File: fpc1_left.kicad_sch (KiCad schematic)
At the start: 1 part

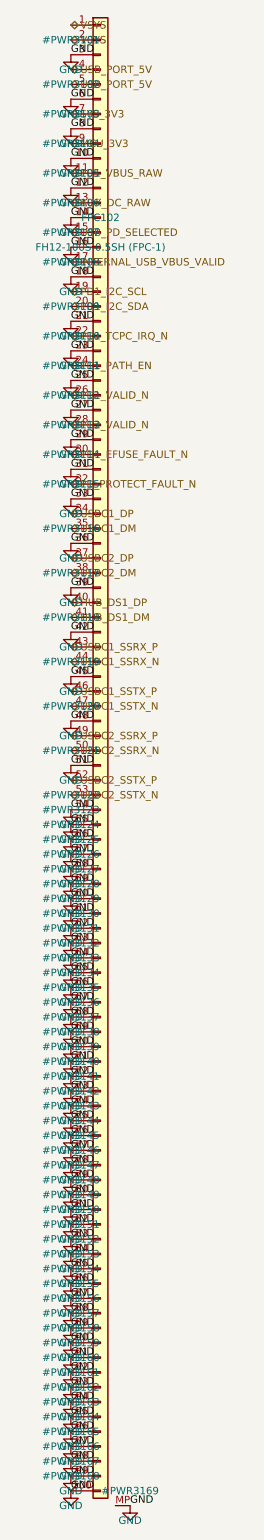
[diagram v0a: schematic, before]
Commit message: Phase 4 deep audit: FH41-68S connectors, placement hygiene, one-shot fixes
Found and fixed four board-killers in the pre-fab audit:

1. Fictional connector: the Hirose FH12 series stops at 60 positions, so
   the 100-pin FH12-100S used for FPC-1/FPC-2 does not exist.  Replaced
   with the FH41-68S-0.5SH(05) (shielded-FFC, 68 positions; FPC-1 uses
   pins 1-53, FPC-2 pins 1-61):
   - new footprint derived from KiCad's FH41-30S (68 signal pads, MP at
     +/-18, 14 SH solder-holds, 38mm body) with SH pads tied to GND
   - new 68-pin symbol (Conn_01x68_FFC_MP), pin maps trimmed to 68
   - fictional FH12-100S footprint/symbol/script removed
   - cable spec updated (68-pin shielded FFC, one type for both)

2. Connector courtyard conflicts: parts sat under connector bodies
   (pads cleared, bodies collided).  Placement now enforces courtyard
   clearance against the connector body; the resolver scans with
   courtyard checks; a double-shift bug that hid re-placed parts' true
   positions was fixed.

3. FPC-3 orientation: the FH12's FPC enters from the +y side; both FPC-3
   connectors faced away from the seam.  FPC105 -> (123.5, 6.5) rot 180,
   FPC106 -> (30, 54) rot 0 so the cable exits the center bottom edge
   and enters the BMS top edge.

4. Original-layout defects: 16 genuine pad-pad shorts (inductor pads
   swallowing caps, passives on each other, parts on mounting holes) and
   23 parts inside the hinge cutouts (physically off the board) are all
   moved to legal spots; zones refilled against the final placement.

New post-build hygiene sweep (fix_board_hygiene.py) uses the final board
text as the geometry oracle, converges to a clean state, and reports
residuals instead of dropping them.

Final DRC: 0 shorts / 0 clearance / 0 hole violations on all four boards
(bms fully clean).  Remaining: courtyard touches around the Mu socket and
M.2 slot (design-inherent moat), chassis-edge copper, zone islands, silk
cosmetics, and unrouted nets (Phase 4b).  Gate: SCHEMATIC R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
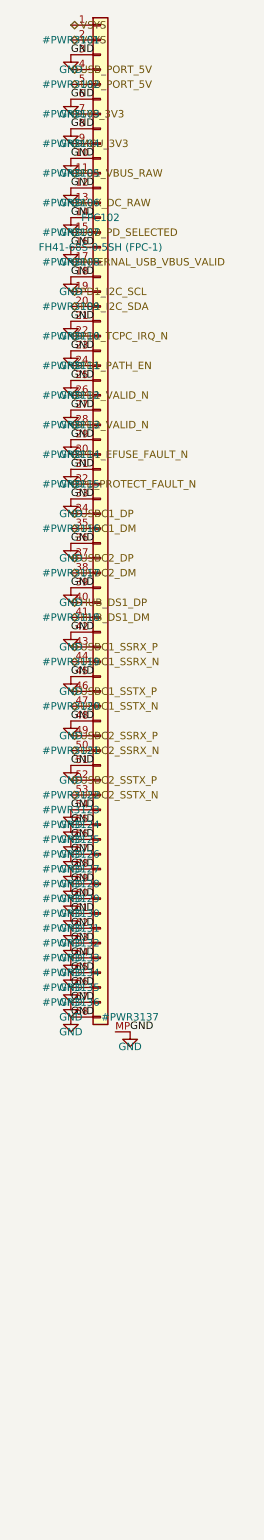
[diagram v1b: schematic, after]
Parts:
- FPC102: value FH12-100S-0.5SH (FPC-1) -> FH41-68S-0.5SH (FPC-1); footprint ducktop2:FH12-100S-0.5SH_1x100-1MP_P0.50mm_Horizontal -> ducktop2:Hirose_FH41-68S-0.5SH_1x68_1MP_1SH_P0.5mm_Horizontal; symbol Conn_01x100_FFC_MP:Conn_01x100_FFC_MP -> Conn_01x68_FFC_MP:Conn_01x68_FFC_MP
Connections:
- net GND: no longer FPC102.100 (Pin_100), FPC102.69 (Pin_69), FPC102.70 (Pin_70), FPC102.71 (Pin_71), FPC102.72 (Pin_72), FPC102.73 (Pin_73), FPC102.74 (Pin_74), FPC102.75 (Pin_75), FPC102.76 (Pin_76), FPC102.77 (Pin_77), FPC102.78 (Pin_78), FPC102.79 (Pin_79), FPC102.80 (Pin_80), FPC102.81 (Pin_81), FPC102.82 (Pin_82), FPC102.83 (Pin_83), FPC102.84 (Pin_84), FPC102.85 (Pin_85), FPC102.86 (Pin_86), FPC102.87 (Pin_87), FPC102.88 (Pin_88), FPC102.89 (Pin_89), FPC102.90 (Pin_90), FPC102.91 (Pin_91), FPC102.92 (Pin_92), FPC102.93 (Pin_93), FPC102.94 (Pin_94), FPC102.95 (Pin_95), FPC102.96 (Pin_96), FPC102.97 (Pin_97), FPC102.98 (Pin_98), FPC102.99 (Pin_99)

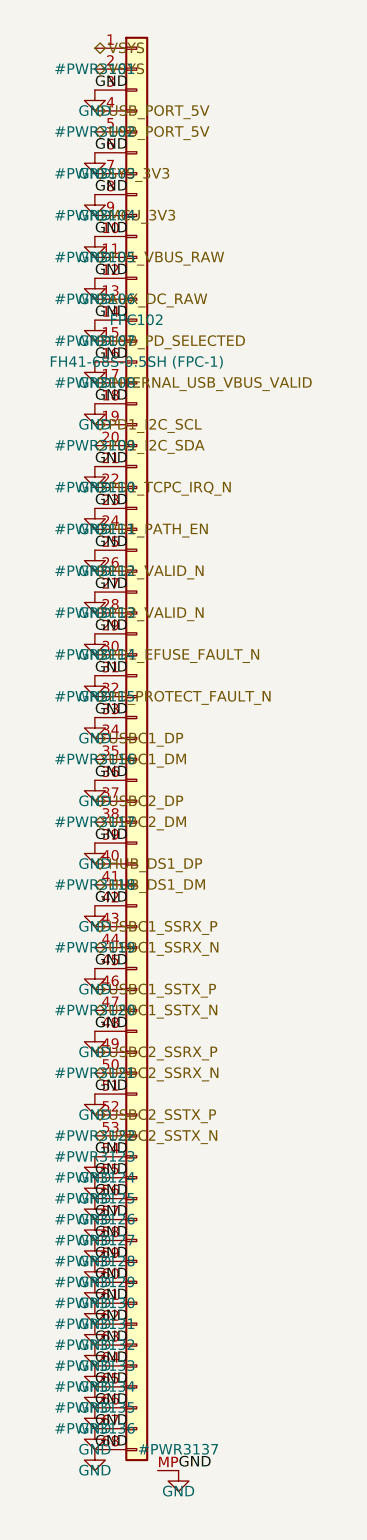
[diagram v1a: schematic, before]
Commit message: Phase 5: second-opinion audit remediation + rebuilt, verified board pipeline
Second-opinion AI audit found A-tier defects; remediation applied and the
board pipeline rebuilt on a known-good base with the fixes it needed:

- electrical: LTC4418IUF symbol pinout corrected (both selectors were
  dead as drawn); center charge cascade (U15 <- U15B, PD1 > PD2 > AUX);
  pack negative never crosses FPC-3, 15-pin FG_VSS return; power-budgeted
  FPC pin maps (0.4 A/pin derate); J12/DS4 completed; AUX source fuse
- FH41-68S footprint: 13 datasheet-correct SH pads + SH pin in symbol
- connector geometry settled against the Hirose FH12 2D drawing: FFC
  enters opposite the solder pins (mouth = local +Y); reversed side-B
  maps are correct for the 180-deg-mounted pairs; rotations set so mouths
  face across every seam
- pipeline (generate_split_boards.py): per-pin pad-net resync from the
  netlists (kills shadow nets for good), netlist-exact name
  normalization, netlist-only part injection (cascade, probe headers),
  zone refill after outline swap, read-before-write race fixed, orphan
  parts dropped loudly, non-zero exit on unresolved overlaps
- monolith board relocated to old/monolith_ducktop2.kicad_pcb (placement
  oracle for the center cut only)

verified end state: 4 boards 0 shorts / 0 clearance / 0 drill, 0 boundary
crossings, 6/6 connectors contract-exact with mouths facing, 0 shadow
nets, gates PASS x4, ERC 0 x4. routing next (499 nets/board).
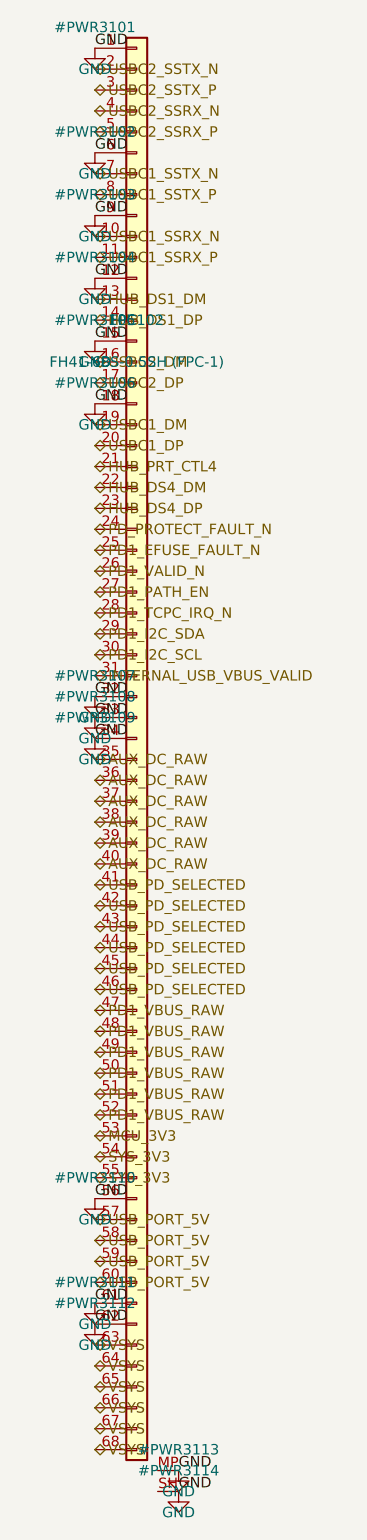
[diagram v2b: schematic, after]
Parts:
- FPC102: MPN (none) -> FH41-68S-0.5SH(05); Manufacturer (none) -> Hirose
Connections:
- net PD2_VALID_N is gone; now on net PD1_TCPC_IRQ_N: FPC102.28 (Pin_28)
- net AUX_DC_RAW: now also FPC102.35 (Pin_35), FPC102.36 (Pin_36), FPC102.37 (Pin_37), FPC102.38 (Pin_38), FPC102.39 (Pin_39), FPC102.40 (Pin_40); no longer FPC102.13 (Pin_13)
- net GND: now also FPC102.1 (Pin_1), FPC102.15 (Pin_15), FPC102.32 (Pin_32), FPC102.34 (Pin_34), FPC102.9 (Pin_9), FPC102.SH; no longer FPC102.10 (Pin_10), FPC102.14 (Pin_14), FPC102.16 (Pin_16), FPC102.21 (Pin_21), FPC102.23 (Pin_23), FPC102.25 (Pin_25), FPC102.27 (Pin_27), FPC102.29 (Pin_29), FPC102.3 (Pin_3), FPC102.31 (Pin_31), FPC102.36 (Pin_36), FPC102.39 (Pin_39), FPC102.42 (Pin_42), FPC102.45 (Pin_45), FPC102.48 (Pin_48), FPC102.51 (Pin_51), FPC102.54 (Pin_54), FPC102.55 (Pin_55), FPC102.57 (Pin_57), FPC102.58 (Pin_58), FPC102.59 (Pin_59), FPC102.60 (Pin_60), FPC102.63 (Pin_63), FPC102.64 (Pin_64), FPC102.65 (Pin_65), FPC102.66 (Pin_66), FPC102.67 (Pin_67), FPC102.68 (Pin_68), FPC102.8 (Pin_8)
- net HUB_DS1_DM: now also FPC102.13 (Pin_13); no longer FPC102.41 (Pin_41)
- net HUB_DS1_DP: now also FPC102.14 (Pin_14); no longer FPC102.40 (Pin_40)
- net INTERNAL_USB_VBUS_VALID: now also FPC102.31 (Pin_31); no longer FPC102.17 (Pin_17)
- net MCU_3V3: now also FPC102.53 (Pin_53); no longer FPC102.9 (Pin_9)
- net PD1_EFUSE_FAULT_N: now also FPC102.25 (Pin_25); no longer FPC102.30 (Pin_30)
- net PD1_I2C_SCL: now also FPC102.30 (Pin_30); no longer FPC102.19 (Pin_19)
- net PD1_I2C_SDA: now also FPC102.29 (Pin_29); no longer FPC102.20 (Pin_20)
- net PD1_PATH_EN: now also FPC102.27 (Pin_27); no longer FPC102.24 (Pin_24)
- net PD1_TCPC_IRQ_N: no longer FPC102.22 (Pin_22)
- net PD1_VBUS_RAW: now also FPC102.47 (Pin_47), FPC102.48 (Pin_48), FPC102.49 (Pin_49), FPC102.50 (Pin_50), FPC102.51 (Pin_51), FPC102.52 (Pin_52); no longer FPC102.11 (Pin_11)
- net PD_PROTECT_FAULT_N: now also FPC102.24 (Pin_24); no longer FPC102.32 (Pin_32)
- net SYS_3V3: now also FPC102.54 (Pin_54), FPC102.55 (Pin_55); no longer FPC102.7 (Pin_7)
- net USBC1_DM: now also FPC102.19 (Pin_19); no longer FPC102.35 (Pin_35)
- net USBC1_DP: now also FPC102.20 (Pin_20); no longer FPC102.34 (Pin_34)
- net USBC1_SSRX_N: now also FPC102.10 (Pin_10); no longer FPC102.44 (Pin_44)
- net USBC1_SSRX_P: now also FPC102.11 (Pin_11); no longer FPC102.43 (Pin_43)
- net USBC1_SSTX_N: now also FPC102.7 (Pin_7); no longer FPC102.47 (Pin_47)
- net USBC1_SSTX_P: now also FPC102.8 (Pin_8); no longer FPC102.46 (Pin_46)
- net USBC2_DM: now also FPC102.16 (Pin_16); no longer FPC102.38 (Pin_38)
- net USBC2_DP: now also FPC102.17 (Pin_17); no longer FPC102.37 (Pin_37)
- net USBC2_SSRX_N: now also FPC102.4 (Pin_4); no longer FPC102.50 (Pin_50)
- net USBC2_SSRX_P: now also FPC102.5 (Pin_5); no longer FPC102.49 (Pin_49)
- net USBC2_SSTX_N: now also FPC102.2 (Pin_2); no longer FPC102.53 (Pin_53)
- net USBC2_SSTX_P: now also FPC102.3 (Pin_3); no longer FPC102.52 (Pin_52)
- net USB_PD_SELECTED: now also FPC102.41 (Pin_41), FPC102.42 (Pin_42), FPC102.43 (Pin_43), FPC102.44 (Pin_44), FPC102.45 (Pin_45), FPC102.46 (Pin_46); no longer FPC102.15 (Pin_15)
- net USB_PORT_5V: now also FPC102.57 (Pin_57), FPC102.58 (Pin_58), FPC102.59 (Pin_59), FPC102.60 (Pin_60); no longer FPC102.4 (Pin_4), FPC102.5 (Pin_5)
- net VSYS: now also FPC102.63 (Pin_63), FPC102.64 (Pin_64), FPC102.65 (Pin_65), FPC102.66 (Pin_66), FPC102.67 (Pin_67), FPC102.68 (Pin_68); no longer FPC102.1 (Pin_1), FPC102.2 (Pin_2)
- new net HUB_DS4_DM: FPC102.22 (Pin_22)
- new net HUB_DS4_DP: FPC102.23 (Pin_23)
- new net HUB_PRT_CTL4: FPC102.21 (Pin_21)

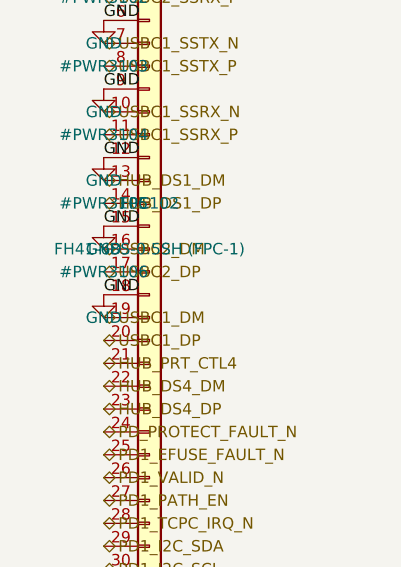
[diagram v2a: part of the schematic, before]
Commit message: get the main boards ready for routing
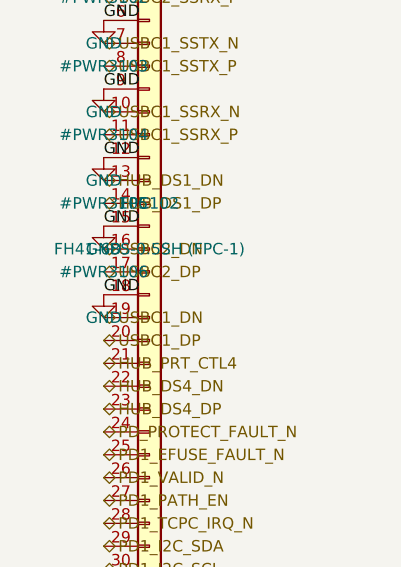
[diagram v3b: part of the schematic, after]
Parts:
- FPC102: MPN FH41-68S-0.5SH(05) -> FH41-68S-0.5SH(28)
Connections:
- net HUB_DS1_DM renamed HUB_DS1_DN
- net HUB_DS4_DM renamed HUB_DS4_DN
- net USBC1_DM renamed USBC1_DN
- net USBC2_DM renamed USBC2_DN
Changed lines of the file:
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@@
   (property "Datasheet" "" (at 59.69 299.72 0) (effects (font (size 1.27 1.27)) (hide yes)))
   (property "Manufacturer" "Hirose" (at 59.69 299.72 0) (effects (font (size 1.27 1.27)) (hide yes)))
-  (property "MPN" "FH41-68S-0.5SH(05)" (at 59.69 299.72 0) (effects (font (size 1.27 1.27)) (hide yes)))
+  (property "MPN" "FH41-68S-0.5SH(28)" (at 59.69 299.72 0) (effects (font (size 1.27 1.27)) (hide yes)))
   (pin "1")
   (pin "2")
@@
   (effects (font (size 1.27 1.27)) (justify left bottom))
 )
-(hierarchical_label "HUB_DS1_DM"
+(hierarchical_label "HUB_DS1_DN"
   (shape bidirectional)
   (at 54.61 294.64 0)
@@
   (effects (font (size 1.27 1.27)) (justify left bottom))
 )
-(hierarchical_label "USBC2_DM"
+(hierarchical_label "USBC2_DN"
   (shape bidirectional)
   (at 54.61 302.26 0)
@@
   (effects (font (size 1.27 1.27)) (justify left bottom))
 )
-(hierarchical_label "USBC1_DM"
+(hierarchical_label "USBC1_DN"
   (shape bidirectional)
   (at 54.61 309.88 0)
@@
   (effects (font (size 1.27 1.27)) (justify left bottom))
 )
-(hierarchical_label "HUB_DS4_DM"
+(hierarchical_label "HUB_DS4_DN"
   (shape bidirectional)
   (at 54.61 317.5 0)

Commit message: fix the center layout and more board issues
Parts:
- added J2430: left power loom, straight-numbered, Connector_Molex:Molex_Micro-Fit_3.0_43045-1212_2x06_P3.00mm_Vertical, symbol Connector_Generic:Conn_02x06_Odd_Even
- added J2441, J2443: main ground strap, Connector_Wire:SolderWirePad_1x01_SMD_5x10mm, symbol Connector:TestPoint
- added R2442, R2443: 0.33, Resistor_SMD:R_0603_1608Metric, symbol Device:R
- FPC102: value FH41-68S-0.5SH (FPC-1) -> Molex5039084120 signal cable; footprint ducktop2:Hirose_FH41-68S-0.5SH_1x68_1MP_1SH_P0.5mm_Horizontal -> ducktop2:Molex_5039084120_1x41_P0.50mm_Horizontal; symbol Conn_01x68_FFC_MP:Conn_01x68_FFC_MP -> Conn_01x41_Signal_SH:Conn_01x41_Signal_SH; MPN FH41-68S-0.5SH(28) -> 5039084120; Manufacturer Hirose -> Molex
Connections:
- net AUX_DC_RAW: now also J2430.4 (Pin_4); no longer FPC102.35 (Pin_35), FPC102.36 (Pin_36), FPC102.37 (Pin_37), FPC102.38 (Pin_38), FPC102.39 (Pin_39), FPC102.40 (Pin_40)
- net GND: now also FPC102.13, FPC102.17, FPC102.20, FPC102.23, FPC102.26, FPC102.29, FPC102.35, FPC102.38, FPC102.41, FPC102.5, J2430.10 (Pin_10), J2430.11 (Pin_11), J2430.12 (Pin_12), J2430.7 (Pin_7), J2430.8 (Pin_8), J2430.9 (Pin_9), J2441.1, J2443.1, R2442.2, R2443.2; no longer FPC102.1 (Pin_1), FPC102.12 (Pin_12), FPC102.15 (Pin_15), FPC102.18 (Pin_18), FPC102.33 (Pin_33), FPC102.34 (Pin_34), FPC102.56 (Pin_56), FPC102.6 (Pin_6), FPC102.61 (Pin_61), FPC102.62 (Pin_62), FPC102.MP, FPC102.SH
- net HUB_DS1_DN: now also FPC102.21; no longer FPC102.13 (Pin_13)
- net HUB_DS1_DP: now also FPC102.22; no longer FPC102.14 (Pin_14)
- net HUB_DS4_DN: now also FPC102.18; no longer FPC102.22 (Pin_22)
- net HUB_DS4_DP: now also FPC102.19; no longer FPC102.23 (Pin_23)
- net HUB_PRT_CTL4: now also FPC102.2; no longer FPC102.21 (Pin_21)
- net INTERNAL_USB_VBUS_VALID: now also FPC102.1; no longer FPC102.31 (Pin_31)
- net MCU_3V3: now also J2430.6 (Pin_6); no longer FPC102.53 (Pin_53)
- net PD1_EFUSE_FAULT_N: now also FPC102.10; no longer FPC102.25 (Pin_25)
- net PD1_I2C_SCL: now also FPC102.16; no longer FPC102.30 (Pin_30)
- net PD1_I2C_SDA: now also FPC102.15; no longer FPC102.29 (Pin_29)
- net PD1_PATH_EN: now also FPC102.12; no longer FPC102.27 (Pin_27)
- net PD1_TCPC_IRQ_N: now also FPC102.14; no longer FPC102.28 (Pin_28)
- net PD1_VALID_N: now also FPC102.11; no longer FPC102.26 (Pin_26)
- net PD1_VBUS_RAW: now also J2430.2 (Pin_2); no longer FPC102.47 (Pin_47), FPC102.48 (Pin_48), FPC102.49 (Pin_49), FPC102.50 (Pin_50), FPC102.51 (Pin_51), FPC102.52 (Pin_52)
- net PD_PROTECT_FAULT_N: now also FPC102.8; no longer FPC102.24 (Pin_24)
- net SYS_3V3: now also J2430.5 (Pin_5); no longer FPC102.54 (Pin_54), FPC102.55 (Pin_55)
- net USBC1_DN: now also FPC102.27; no longer FPC102.19 (Pin_19)
- net USBC1_DP: now also FPC102.28; no longer FPC102.20 (Pin_20)
- net USBC1_SSRX_N: now also FPC102.39; no longer FPC102.10 (Pin_10)
- net USBC1_SSRX_P: now also FPC102.40; no longer FPC102.11 (Pin_11)
- net USBC1_SSTX_N: now also FPC102.36; no longer FPC102.7 (Pin_7)
- net USBC1_SSTX_P: now also FPC102.37; no longer FPC102.8 (Pin_8)
- net USBC2_DN: now also FPC102.24; no longer FPC102.16 (Pin_16)
- net USBC2_DP: now also FPC102.25; no longer FPC102.17 (Pin_17)
- net USBC2_SSRX_N: now also FPC102.33; no longer FPC102.4 (Pin_4)
- net USBC2_SSRX_P: now also FPC102.34; no longer FPC102.5 (Pin_5)
- net USBC2_SSTX_N: now also FPC102.30; no longer FPC102.2 (Pin_2)
- net USBC2_SSTX_P: now also FPC102.31; no longer FPC102.3 (Pin_3)
- net USB_PD_SELECTED: now also J2430.3 (Pin_3); no longer FPC102.41 (Pin_41), FPC102.42 (Pin_42), FPC102.43 (Pin_43), FPC102.44 (Pin_44), FPC102.45 (Pin_45), FPC102.46 (Pin_46)
- net VSYS: now also J2430.1 (Pin_1); no longer FPC102.63 (Pin_63), FPC102.64 (Pin_64), FPC102.65 (Pin_65), FPC102.66 (Pin_66), FPC102.67 (Pin_67), FPC102.68 (Pin_68)
- removed net USB_PORT_5V: FPC102.57 (Pin_57), FPC102.58 (Pin_58), FPC102.59 (Pin_59), FPC102.60 (Pin_60)
- new net FPC102_SHELL: FPC102.SH, R2442.1, R2443.1
- new net PD2_SOURCE_PG: FPC102.6
- new net SERVICE_MUX_RESET_N: FPC102.7
- new net USB_J11_PERMIT: FPC102.4
- new net USB_J12_PERMIT: FPC102.3
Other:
- note added: "Both ground straps must be fitted before the signal cable. Keep raw and protected battery returns separate from these main-board grounds."
- note added: "Power uses the separate rated looms. The signal cable carries no positive supply rails."
- note added: "The shell uses two parallel 0.33 ohm returns at each connector. Numbered ground conductors connect directly to the local ground plane."
